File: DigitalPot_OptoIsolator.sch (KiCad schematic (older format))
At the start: 18 parts, among them J1 DIN-5, J2 5-Way Pin Header, U1 TLP2361, U2 TLP2361, U3 TLP2361, U4 FODM8801

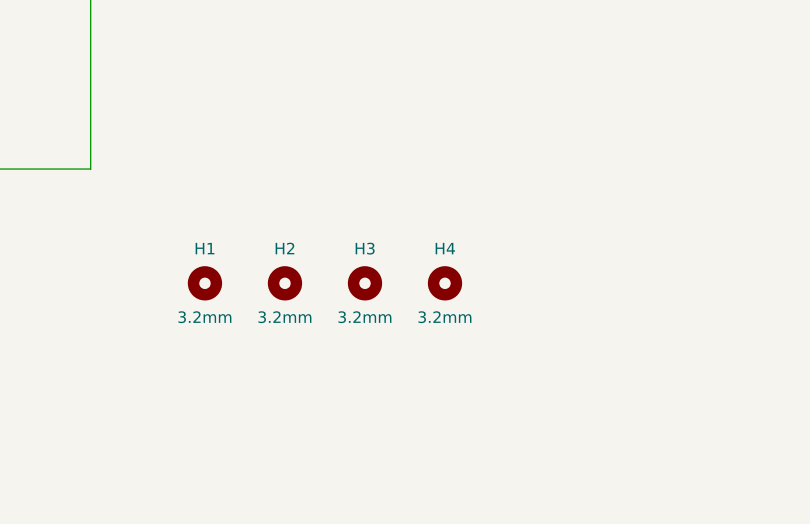
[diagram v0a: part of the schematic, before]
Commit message: Made board smaller to fit the box, removed two mounting screws, made central hole larger diameter so it can be used as a marking hole.
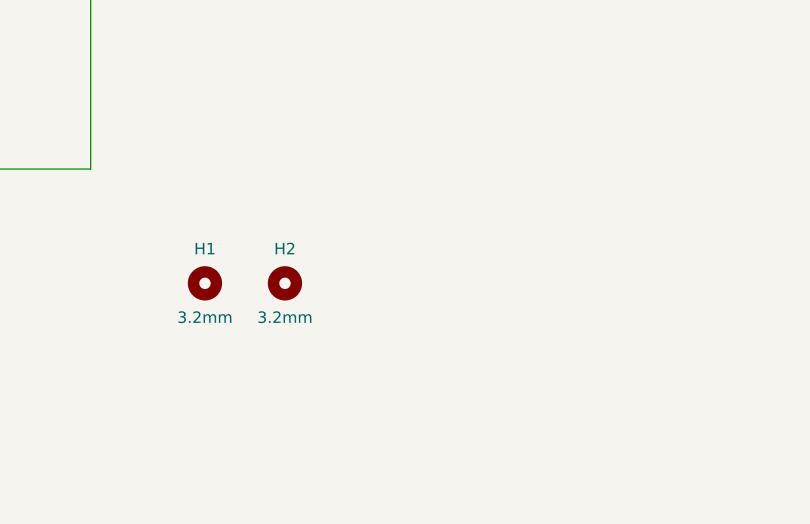
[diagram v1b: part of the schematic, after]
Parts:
- removed H3, H4: 3.2mm, MountingHole:MountingHole_3.2mm_M3, symbol Mechanical:MountingHole
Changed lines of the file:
@@
 EESchema Schematic File Version 4
 LIBS:DigitalPot_OptoIsolator-cache
-EELAYER 29 0
+EELAYER 30 0
 EELAYER END
 $Descr A4 11693 8268
 encoding utf-8
 Sheet 1 1
-Title ""
-Date ""
-Rev ""
-Comp ""
+Title "Optocoupler for digital pot"
+Date "2019-08-08"
+Rev "v1.1"
+Comp "King's College London"
 Comment1 ""
 Comment2 ""
@@
 	1    0    0    -1
 $EndComp
-$Comp
-L Mechanical:MountingHole H3
-U 1 1 5D374824
-P 9200 5000
-F 0 "H3" H 9200 5150 50  0000 C CNN
-F 1 "3.2mm" H 9200 4850 50  0000 C CNN
-F 2 "MountingHole:MountingHole_3.2mm_M3" H 9200 5000 50  0001 C CNN
-F 3 "~" H 9200 5000 50  0001 C CNN
-	1    9200 5000
-	1    0    0    -1
-$EndComp
-$Comp
-L Mechanical:MountingHole H4
-U 1 1 5D374AEC
-P 9550 5000
-F 0 "H4" H 9550 5150 50  0000 C CNN
-F 1 "3.2mm" H 9550 4850 50  0000 C CNN
-F 2 "MountingHole:MountingHole_3.2mm_M3" H 9550 5000 50  0001 C CNN
-F 3 "~" H 9550 5000 50  0001 C CNN
-	1    9550 5000
-	1    0    0    -1
-$EndComp
